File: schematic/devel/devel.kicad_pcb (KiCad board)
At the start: 2 copper layers, 41 parts, among them J1 CONN_PWR, J2 CONN_X1, J3 CONN_Y2, J4 CONN_X2, J5 CONN_Y1, U1 LM317_SOT223, U2 LM337_SOT223, U3 REF5010IDGK, U4 OPA4197

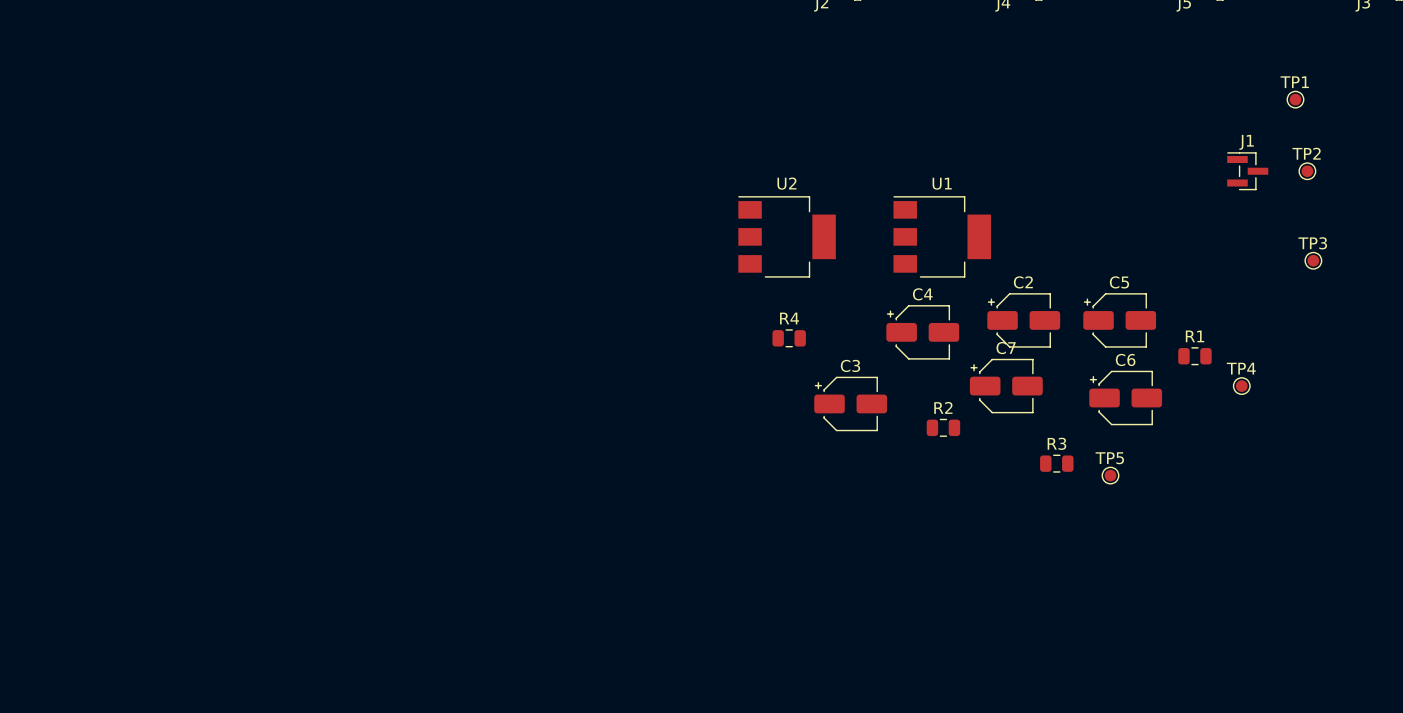
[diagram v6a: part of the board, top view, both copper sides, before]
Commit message: completed sublayout of power input
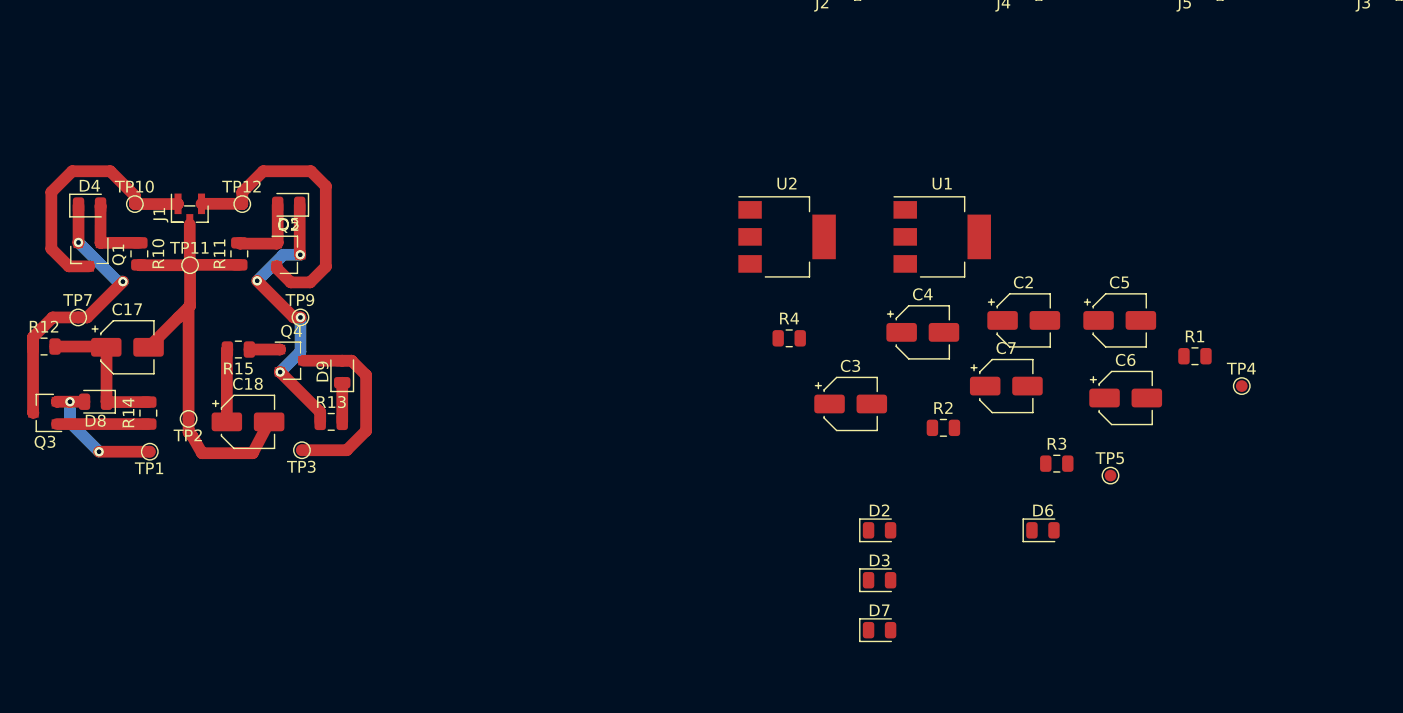
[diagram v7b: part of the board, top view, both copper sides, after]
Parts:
- added C17: 100u, Capacitor_SMD:CP_Elec_4x3.9, F.Cu at (44.3, 106.4)
- added C18: 100u, Capacitor_SMD:CP_Elec_4x3.9, F.Cu at (54.6, 112.8)
- added D2: 1N4001, Diode_SMD:D_0805_2012Metric, F.Cu at (108.4, 122.0)
- added D3: 1N4001, Diode_SMD:D_0805_2012Metric, F.Cu at (108.4, 126.3)
- added D4: D_Zener_Small, Diode_SMD:D_0805_2012Metric, F.Cu at (41.1, 94.4)
- added D5: D_Zener_Small, Diode_SMD:D_0805_2012Metric, F.Cu at (58.1, 94.3)
- added D6: 1N4001, Diode_SMD:D_0805_2012Metric, F.Cu at (122.3, 122.0)
- added D7: 1N4001, Diode_SMD:D_0805_2012Metric, F.Cu at (108.4, 130.5)
- added D8: D_Small, Diode_SMD:D_0805_2012Metric, F.Cu at (41.6, 111.1)
- added D9: D_Small, Diode_SMD:D_0805_2012Metric, F.Cu at (62.6, 108.5)
- added Q1: Q_PMOS_GSD, Package_TO_SOT_SMD:SOT-23, F.Cu at (41.1, 98.5)
- added Q2: Q_NMOS_GSD, Package_TO_SOT_SMD:SOT-23, F.Cu at (58.0, 98.6)
- added Q3: Q_PMOS_GSD, Package_TO_SOT_SMD:SOT-23, F.Cu at (37.3, 112.0)
- added Q4: Q_NMOS_GSD, Package_TO_SOT_SMD:SOT-23, F.Cu at (58.3, 107.6)
- added R10: 100k, Resistor_SMD:R_0805_2012Metric, F.Cu at (45.3, 98.5)
- added R11: 100k, Resistor_SMD:R_0805_2012Metric, F.Cu at (53.8, 98.5)
- added R12: 22, Resistor_SMD:R_0805_2012Metric, F.Cu at (37.2, 106.4)
- added R13: 22, Resistor_SMD:R_0805_2012Metric, F.Cu at (61.7, 112.8)
- added R14: 100, Resistor_SMD:R_0805_2012Metric, F.Cu at (46.1, 112.0)
- added R15: 100, Resistor_SMD:R_0805_2012Metric, F.Cu at (53.8, 106.6)
- added TP10: TestPoint, TestPoint:TestPoint_Pad_D1.0mm, F.Cu at (45.0, 94.2)
- added TP11: TestPoint, TestPoint:TestPoint_Pad_D1.0mm, F.Cu at (49.7, 99.4)
- added TP12: TestPoint, TestPoint:TestPoint_Pad_D1.0mm, F.Cu at (54.1, 94.2)
- added TP7: TestPoint, TestPoint:TestPoint_Pad_D1.0mm, F.Cu at (40.1, 103.9)
- added TP9: TestPoint, TestPoint:TestPoint_Pad_D1.0mm, F.Cu at (59.1, 103.9)
- J1: footprint Connector_PinHeader_1.00mm:PinHeader_1x03_P1.00mm_Vertical_SMD_Pin1Left -> Connector_PinHeader_1.00mm:PinHeader_1x03_P1.00mm_Vertical_SMD_Pin1Right
- R2, R3: value 1050 -> 980
- moved TP1 102.0 mm to (46.2, 115.3), turned to 180 degrees
- moved TP2 97.6 mm to (49.5, 112.5), turned to 180 degrees
- moved J1 90.1 mm to (49.6, 95.1), turned to 90 degrees
- moved TP3 87.6 mm to (59.2, 115.2), turned to 180 degrees
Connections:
- J1 pad 1: +15V -> Net-(J1-Pad1)
- J1 pad 3: -15V -> Net-(J1-Pad3)
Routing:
- net GND: track 14.6 -> 55.7 mm
- net Net-(J1-Pad3): track 0.00 -> 25.2 mm
- net Net-(D4-Pad1): track 0.00 -> 25.1 mm, vias 0 -> 2
- net Net-(D5-Pad1): track 0.00 -> 24.9 mm, vias 0 -> 4
- net Net-(J1-Pad1): track 0.00 -> 21.8 mm
- net -15V: track 0.00 -> 16.7 mm
- net Net-(C17-Pad1): track 0.00 -> 12.6 mm
- net +15V: track 2.43 -> 14.4 mm, vias 0 -> 2
- net Net-(C18-Pad1): track 0.00 -> 9.51 mm
- net Net-(Q3-Pad1): track 0.00 -> 7.78 mm
- net Net-(D4-Pad2): track 0.00 -> 6.61 mm
- net Net-(D5-Pad2): track 0.00 -> 6.55 mm
- net Net-(Q4-Pad1): track 0.00 -> 2.60 mm

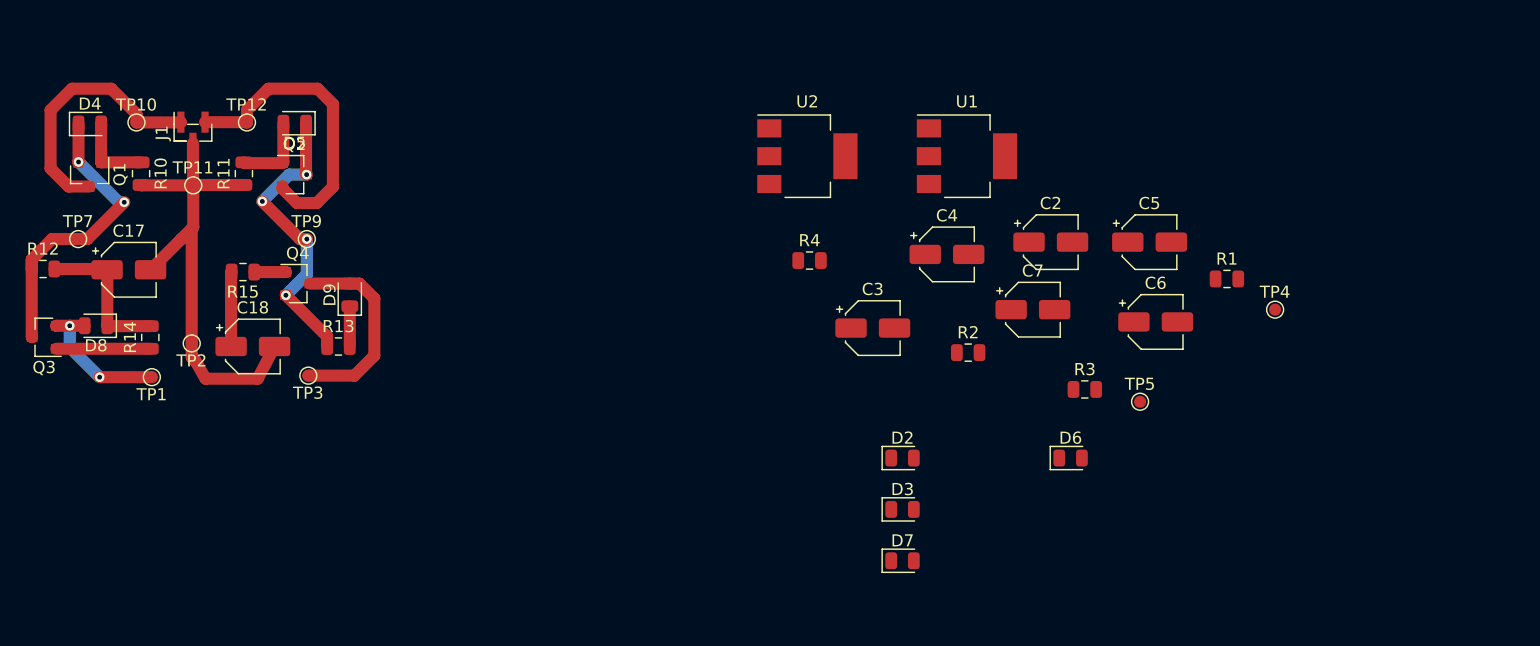
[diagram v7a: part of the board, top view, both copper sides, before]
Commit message: completed pcb sublayouts
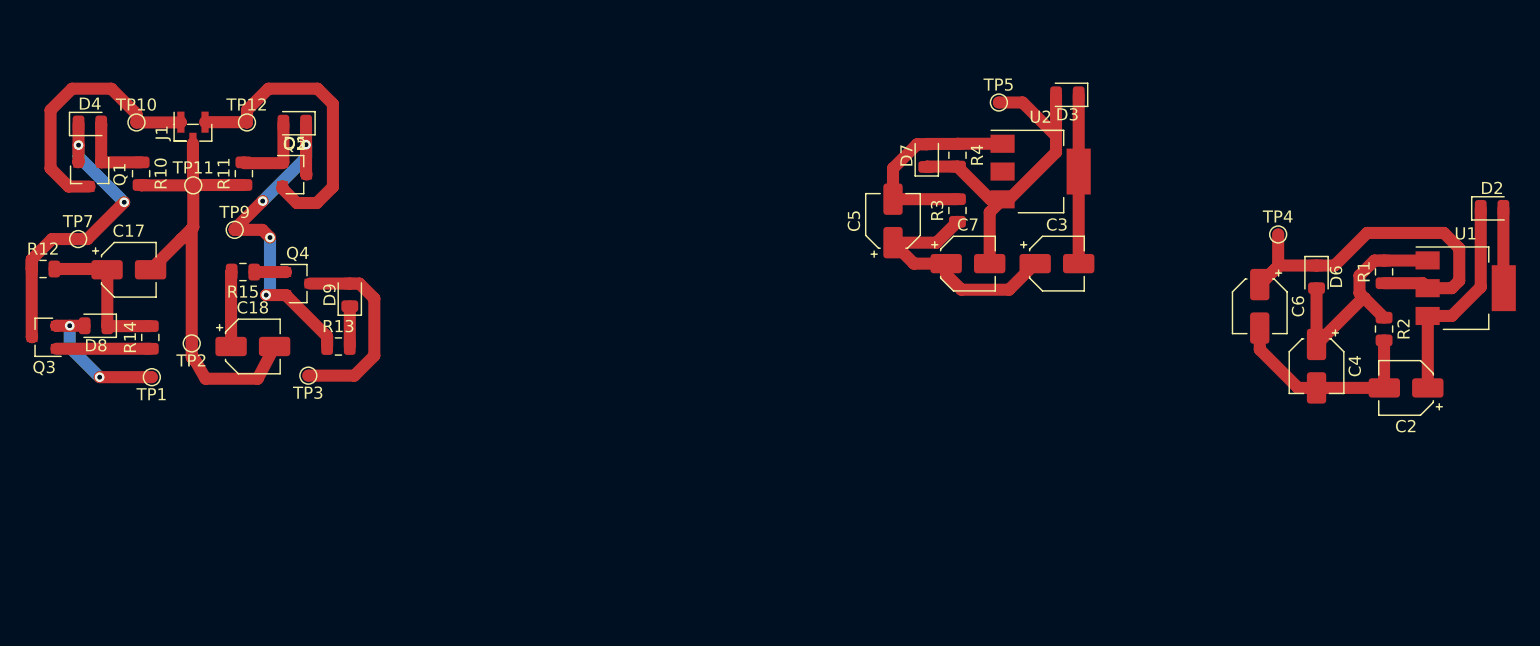
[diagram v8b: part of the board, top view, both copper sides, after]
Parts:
- moved D2 53.0 mm to (157.1, 101.3)
- moved U1 42.7 mm to (155.0, 108.0)
- moved D3 36.9 mm to (122.0, 91.9), turned to 180 degrees
- moved R2 34.5 mm to (148.2, 111.3), turned to 270 degrees
- moved D7 33.6 mm to (110.4, 97.0), turned to 90 degrees
- moved C4 32.0 mm to (142.6, 114.4), turned to 270 degrees
- moved C2 31.8 mm to (150.0, 116.2), turned to 180 degrees
- moved TP5 27.4 mm to (116.3, 92.6)
- moved D6 25.3 mm to (142.6, 107.0), turned to 270 degrees
- moved C5 21.3 mm to (107.6, 102.4), turned to 90 degrees
- moved U2 19.3 mm to (119.8, 98.3)
- moved R3 18.2 mm to (112.9, 101.5), turned to 90 degrees
- moved C3 16.1 mm to (121.1, 105.9)
- moved R4 15.0 mm to (112.9, 96.9), turned to 270 degrees
- moved R1 13.0 mm to (148.2, 106.6), turned to 90 degrees
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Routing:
- net +12V: track 0.00 -> 39.5 mm
- net GND: track 55.7 -> 93.9 mm
- net -12V: track 0.00 -> 29.8 mm
- net Net-(C4-Pad1): track 0.00 -> 20.7 mm
- net +15V: track 14.4 -> 32.2 mm
- net Net-(C5-Pad2): track 0.00 -> 17.8 mm
- net -15V: track 16.7 -> 30.7 mm
- net Net-(D5-Pad1): track 24.9 -> 29.2 mm
- net Net-(D4-Pad1): track 25.1 -> 26.2 mm
